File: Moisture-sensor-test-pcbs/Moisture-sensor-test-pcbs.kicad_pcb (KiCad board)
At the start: 2 copper layers, 87 x 82.3 mm, 31 parts

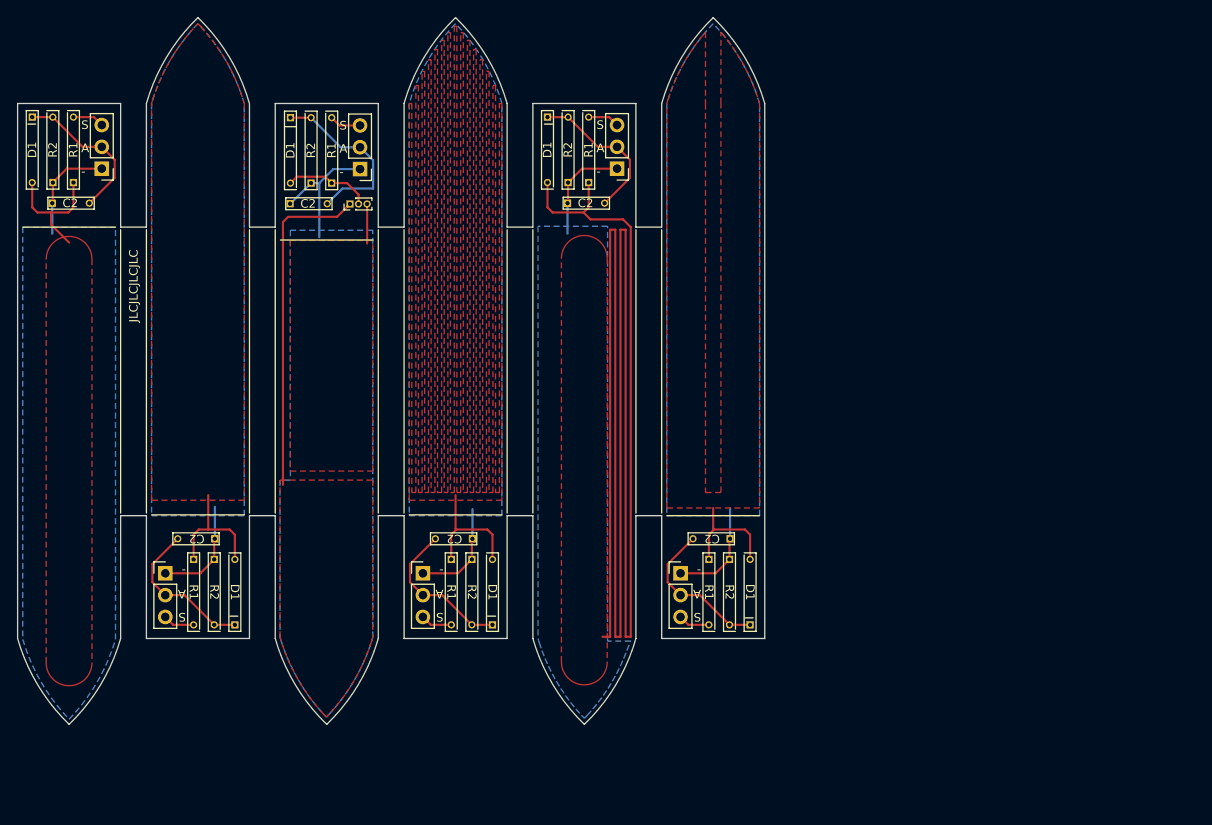
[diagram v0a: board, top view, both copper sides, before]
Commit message: Board: Change from 2-layer to 4-layer board
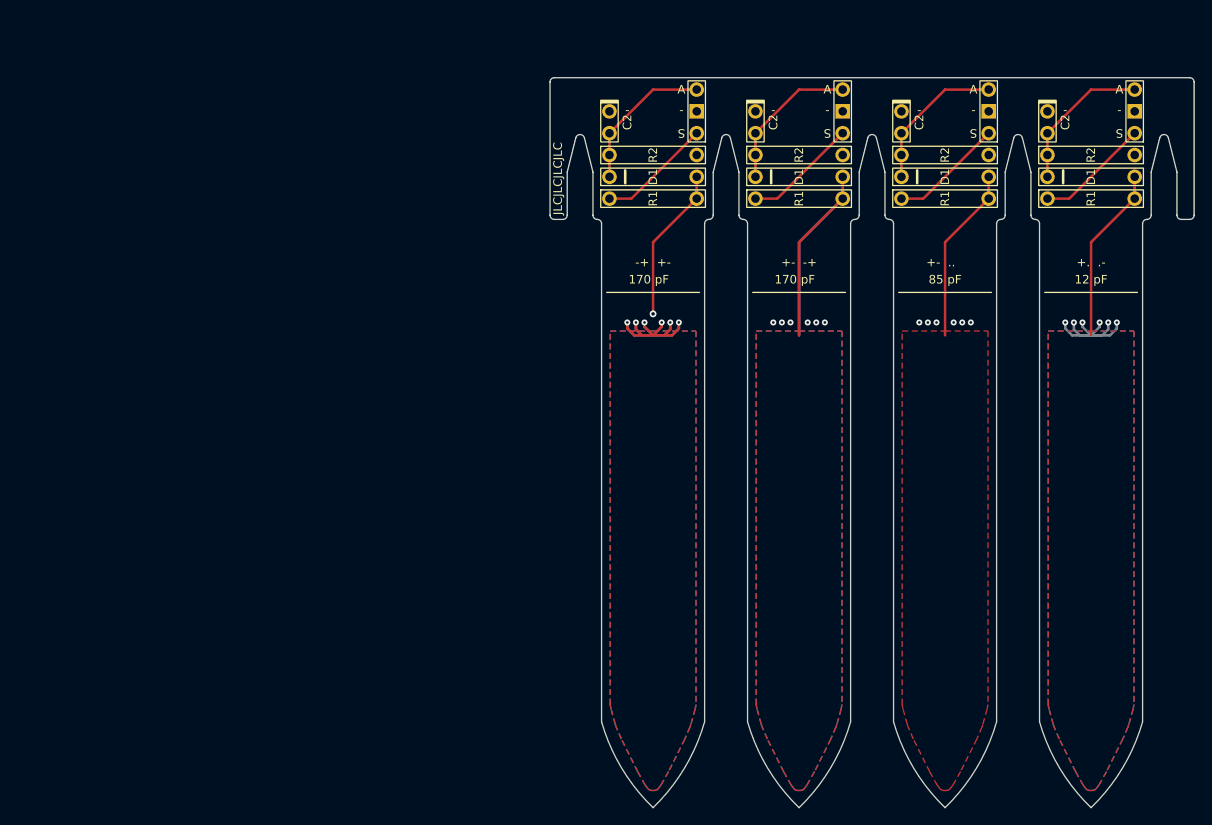
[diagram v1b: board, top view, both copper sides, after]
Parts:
- removed the C2 at (105.9, 110.8)
- removed the C2 at (95.1, 71.5)
- removed the C2 at (155.1, 71.5)
- removed the C2 at (165.9, 110.8)
- removed the C2 at (135.9, 110.8)
- removed the C2 at (122.8, 71.6)
- removed the D1 at (118.8, 65.5)
- removed the D1 at (88.7, 65.4)
- removed the D1 at (148.7, 65.4)
- removed the D1 at (112.3, 116.9)
- removed the D1 at (142.3, 116.9)
- removed the D1 at (172.3, 116.9)
- removed the R1 at (153.5, 65.4)
- removed the R1 at (93.5, 65.4)
- removed the R1 at (137.5, 116.9)
- removed the R1 at (123.6, 65.5)
- removed the R1 at (107.5, 116.9)
- removed the R1 at (167.5, 116.9)
- removed the R2 at (169.9, 116.9)
- removed the R2 at (109.9, 116.9)
- removed the R2 at (121.2, 65.5)
- removed the R2 at (91.1, 65.4)
- removed the R2 at (139.9, 116.9)
- removed the R2 at (151.1, 65.4)
- removed REF** (x6): PinHeader_1x03_P2.54mm_Vertical, Connector_PinHeader_2.54mm:PinHeader_1x03_P2.54mm_Vertical
- removed REF**: PinHeader_1x03_P1.00mm_Vertical, Connector_PinHeader_1.00mm:PinHeader_1x03_P1.00mm_Vertical
- added C2: C, ThroughHoleParts:Capacitor, F.Cu at (189.9, 62.2)
- added C2: C, ThroughHoleParts:Capacitor, F.Cu at (206.9, 62.2)
- added C2: C, ThroughHoleParts:Capacitor, F.Cu at (155.9, 62.2)
- added C2: C, ThroughHoleParts:Capacitor, F.Cu at (172.9, 62.2)
- added D1: D, ThroughHoleParts:Diode, F.Cu at (178.0, 68.5)
- added D1: D, ThroughHoleParts:Diode, F.Cu at (161.0, 68.5)
- added D1: D, ThroughHoleParts:Diode, F.Cu at (195.0, 68.5)
- added D1: D, ThroughHoleParts:Diode, F.Cu at (212.0, 68.5)
- added J1: Conn_01x03_Pin, ThroughHoleParts:PinHeader1x03, F.Cu at (166.1, 60.9)
- added J1: Conn_01x03_Pin, ThroughHoleParts:PinHeader1x03, F.Cu at (200.1, 60.9)
- added J1: Conn_01x03_Pin, ThroughHoleParts:PinHeader1x03, F.Cu at (183.1, 60.9)
- added J1: Conn_01x03_Pin, ThroughHoleParts:PinHeader1x03, F.Cu at (217.1, 60.9)
- added R1: R, ThroughHoleParts:Resistor, F.Cu at (161.0, 71.1)
- added R1: R, ThroughHoleParts:Resistor, F.Cu at (195.0, 71.1)
- added R1: R, ThroughHoleParts:Resistor, F.Cu at (178.0, 71.1)
- added R1: R, ThroughHoleParts:Resistor, F.Cu at (212.0, 71.1)
- added R2: R, ThroughHoleParts:Resistor, F.Cu at (161.0, 66.0)
- added R2: R, ThroughHoleParts:Resistor, F.Cu at (212.0, 66.0)
- added R2: R, ThroughHoleParts:Resistor, F.Cu at (178.0, 66.0)
- added R2: R, ThroughHoleParts:Resistor, F.Cu at (195.0, 66.0)
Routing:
- net /CapV: track 371.1 -> 102.8 mm, vias 0 -> 1
- net /GND: track 78.0 -> 0.00 mm
- net GND: track 0.00 -> 51.6 mm, vias 0 -> 24
- net /ADC: track 110.9 -> 69.4 mm
- net /SWS: track 22.1 -> 53.3 mm
- added copper zone on B.Cu, net /CapV
- added copper zone on In1.Cu, net /CapV
- added copper zone on In2.Cu, net /CapV
- added copper zone on B.Cu, net GND
- added copper zone on F.Cu, net GND
- added copper zone on In1.Cu, net GND
- added copper zone on In2.Cu, net GND
- removed copper zone on B.Cu, net /GND
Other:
- board size 87 x 82.3 mm -> 75 x 85 mm
- copper layers 2 -> 4
- board text added: "+- -+"
- board text added: "+- .."
- board text added: "+. .-"
- board text added: "-+ +-"
- board text added: "12 pF"
- board text added: "170 pF"
- board text added: "85 pF"
